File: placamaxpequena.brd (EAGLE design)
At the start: 10 x 15 mm, 7 parts

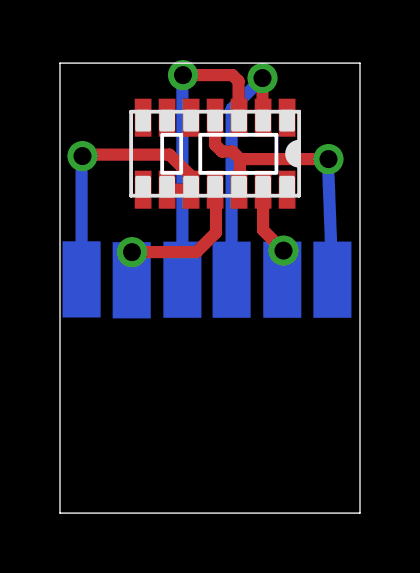
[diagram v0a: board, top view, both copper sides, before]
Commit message: reduced the board
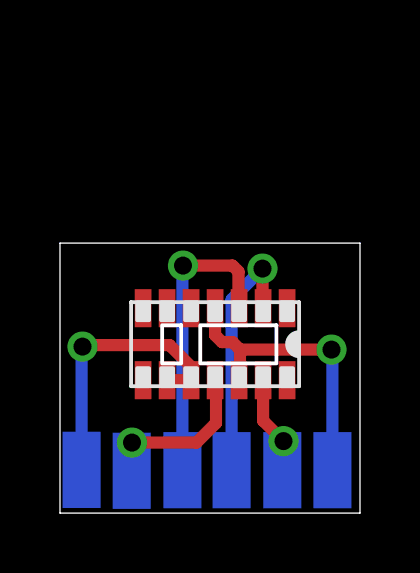
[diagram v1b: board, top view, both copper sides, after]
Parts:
- moved GND 6.35 mm to (9.08, 1.43)
- moved INT 6.35 mm to (7.41, 1.43)
- moved SCL 6.35 mm to (5.72, 1.43)
- moved SDA 6.35 mm to (4.08, 1.43)
- moved 1V8 6.35 mm to (2.39, 1.41)
- moved 3V3 6.35 mm to (0.72, 1.44)
- moved U$1 6.35 mm to (7.85, 3.72)
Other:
- board size 10 x 15 mm -> 10 x 9 mm
